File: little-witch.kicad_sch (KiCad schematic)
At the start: 31 parts, among them J1 GCT-USB4105, J3 Conn_ARM_SWD_TagConnect_TC203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, J4 GCT-USB4105, J5 Conn_02x20_Odd_Even, J6 BOOT0_SEL, SW1 SW_Push, U1 CH32V307RCT6, Y1 SIT8008BI-73-33N-25.000000

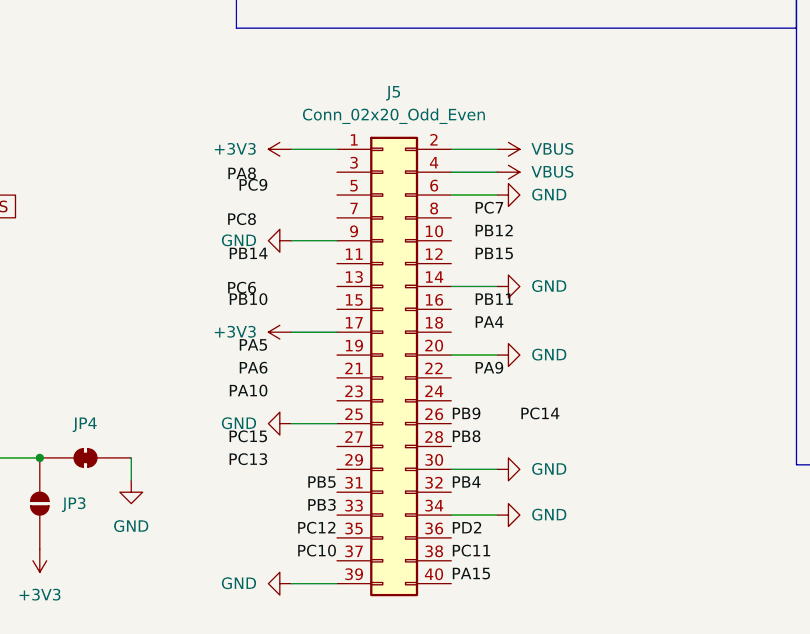
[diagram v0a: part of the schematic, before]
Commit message: More GPIO routing
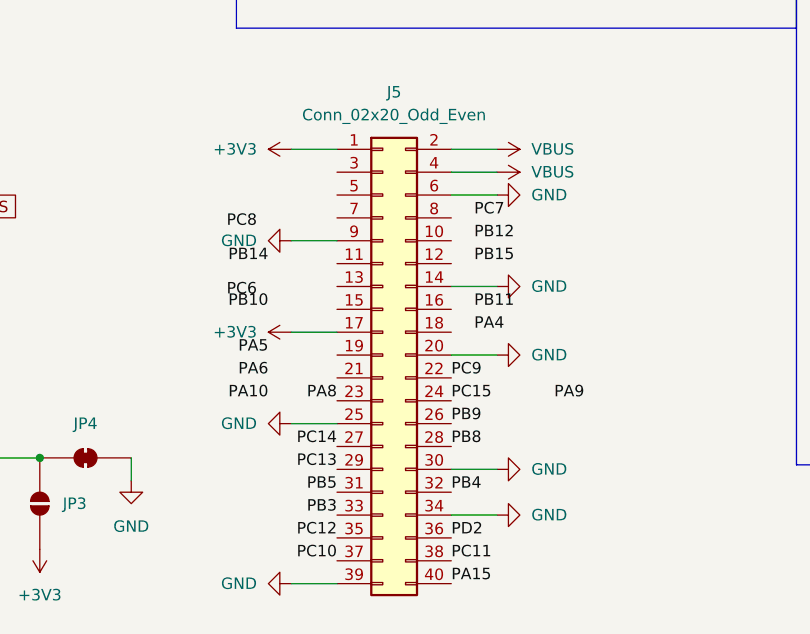
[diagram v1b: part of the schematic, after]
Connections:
- net PA8: now also J5.23 (Pin_23)
- net PC13: now also J5.29 (Pin_29)
- net PC14: now also J5.27 (Pin_27)
- net PC15: now also J5.24 (Pin_24)
- net PC9: now also J5.22 (Pin_22)
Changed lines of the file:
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@@
 	)
 	(label "PC13"
-		(at 162.56 139.7 180)
+		(at 170.18 139.7 180)
 		(effects
 			(font
@@
 	)
 	(label "PC14"
-		(at 190.5 134.62 0)
-		(effects
-			(font
-				(size 1.27 1.27)
-			)
-			(justify left bottom)
+		(at 170.18 137.16 180)
+		(effects
+			(font
+				(size 1.27 1.27)
+			)
+			(justify right bottom)
 		)
 	)
@@
 	)
 	(label "PC15"
-		(at 162.56 137.16 180)
-		(effects
-			(font
-				(size 1.27 1.27)
-			)
-			(justify right bottom)
+		(at 182.88 132.08 0)
+		(effects
+			(font
+				(size 1.27 1.27)
+			)
+			(justify left bottom)
 		)
 	)
@@
 	)
 	(label "PA9"
-		(at 185.42 129.54 0)
+		(at 194.31 132.08 0)
 		(effects
 			(font
@@
 	)
 	(label "PA8"
-		(at 161.29 107.95 180)
+		(at 170.18 132.08 180)
 		(effects
 			(font
@@
 	)
 	(label "PC9"
-		(at 162.56 109.22 180)
-		(effects
-			(font
-				(size 1.27 1.27)
-			)
-			(justify right bottom)
-		)
-	)
+		(at 182.88 129.54 0)
+		(effects
+			(font
+				(size 1.27 1.27)
+			)
+			(justify left bottom)
+		)
+	)

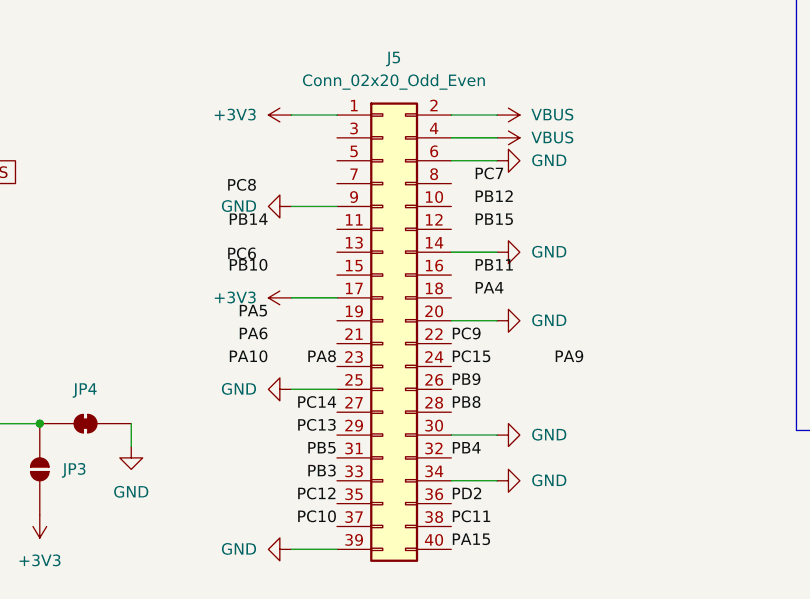
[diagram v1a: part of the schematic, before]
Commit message: Yet more GPIO routing
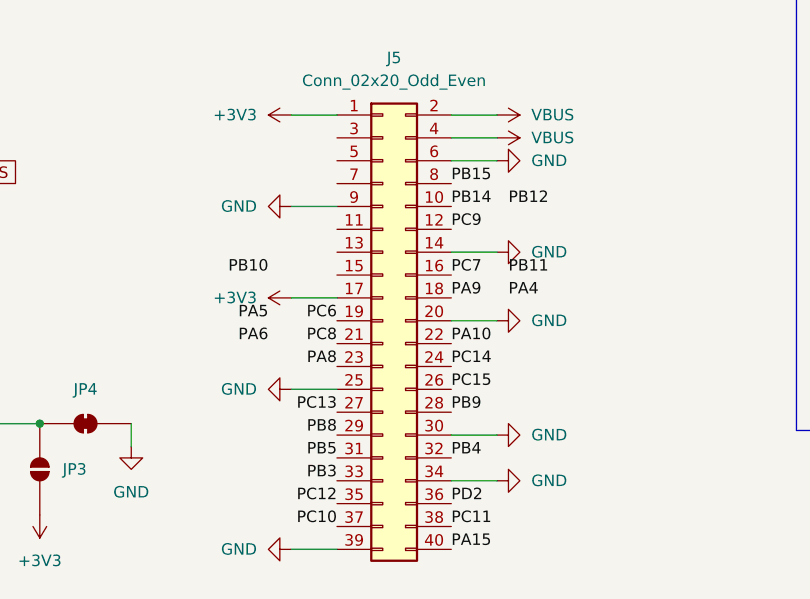
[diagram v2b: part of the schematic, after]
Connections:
- net PA10: now also J5.22 (Pin_22)
- net PA9: now also J5.18 (Pin_18)
- net PB14: now also J5.10 (Pin_10)
- net PB15: now also J5.8 (Pin_8)
- net PB8: now also J5.29 (Pin_29); no longer J5.28 (Pin_28)
- net PB9: now also J5.28 (Pin_28); no longer J5.26 (Pin_26)
- net PC13: now also J5.27 (Pin_27); no longer J5.29 (Pin_29)
- net PC14: now also J5.24 (Pin_24); no longer J5.27 (Pin_27)
- net PC15: now also J5.26 (Pin_26); no longer J5.24 (Pin_24)
- net PC6: now also J5.19 (Pin_19)
- net PC7: now also J5.16 (Pin_16)
- net PC8: now also J5.21 (Pin_21)
- net PC9: now also J5.12 (Pin_12); no longer J5.22 (Pin_22)
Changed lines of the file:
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@@
+		)
+	)
+	(label "PB9"
+		(at 182.88 137.16 0)
+		(effects
+			(font
+				(size 1.27 1.27)
+			)
+			(justify left bottom)
 		)
 	)
@@
 		)
 	)
-	(label "PC13"
-		(at 170.18 139.7 180)
-		(effects
-			(font
-				(size 1.27 1.27)
-			)
-			(justify right bottom)
-		)
-	)
 	(label "PC15"
 		(at 66.04 168.91 180)
@@
 	)
 	(label "PA4"
-		(at 185.42 124.46 0)
+		(at 189.23 124.46 0)
 		(effects
 			(font
@@
 	)
 	(label "PC6"
-		(at 161.29 120.65 180)
+		(at 170.18 127 180)
 		(effects
 			(font
@@
 		)
 	)
-	(label "PC14"
-		(at 170.18 137.16 180)
-		(effects
-			(font
-				(size 1.27 1.27)
-			)
-			(justify right bottom)
-		)
-	)
 	(label "PC8"
 		(at 66.04 151.13 180)
@@
 		)
 	)
+	(label "PB8"
+		(at 170.18 139.7 180)
+		(effects
+			(font
+				(size 1.27 1.27)
+			)
+			(justify right bottom)
+		)
+	)
 	(label "PA6"
 		(at 104.14 102.87 0)
@@
 		)
 	)
-	(label "PC15"
-		(at 182.88 132.08 0)
-		(effects
-			(font
-				(size 1.27 1.27)
-			)
-			(justify left bottom)
-		)
-	)
 	(label "PA10"
 		(at 104.14 113.03 0)
@@
 		)
 	)
-	(label "PB8"
-		(at 182.88 137.16 0)
-		(effects
-			(font
-				(size 1.27 1.27)
-			)
-			(justify left bottom)
-		)
-	)
 	(label "PA10"
-		(at 162.56 132.08 180)
-		(effects
-			(font
-				(size 1.27 1.27)
-			)
-			(justify right bottom)
+		(at 182.88 129.54 0)
+		(effects
+			(font
+				(size 1.27 1.27)
+			)
+			(justify left bottom)
 		)
 	)
 	(label "PA9"
-		(at 194.31 132.08 0)
+		(at 182.88 124.46 0)
 		(effects
 			(font
@@
 	)
 	(label "PC7"
-		(at 185.42 111.76 0)
+		(at 182.88 121.92 0)
 		(effects
 			(font
@@
 	)
 	(label "PB15"
-		(at 185.42 116.84 0)
+		(at 182.88 111.76 0)
 		(effects
 			(font
@@
 	)
 	(label "PB12"
-		(at 185.42 114.3 0)
+		(at 189.23 114.3 0)
 		(effects
 			(font
@@
 		)
 	)
-	(label "PB9"
-		(at 182.88 134.62 0)
-		(effects
-			(font
-				(size 1.27 1.27)
-			)
-			(justify left bottom)
-		)
-	)
 	(label "PB11"
-		(at 185.42 121.92 0)
+		(at 189.23 121.92 0)
 		(effects
 			(font
@@
 		)
 	)
+	(label "PC13"
+		(at 170.18 137.16 180)
+		(effects
+			(font
+				(size 1.27 1.27)
+			)
+			(justify right bottom)
+		)
+	)
 	(label "PB2"
 		(at 104.14 135.89 0)
@@
 	)
 	(label "PC8"
-		(at 161.29 113.03 180)
+		(at 170.18 129.54 180)
 		(effects
 			(font
@@
 	)
 	(label "PB14"
-		(at 162.56 116.84 180)
-		(effects
-			(font
-				(size 1.27 1.27)
-			)
-			(justify right bottom)
+		(at 182.88 114.3 0)
+		(effects
+			(font
+				(size 1.27 1.27)
+			)
+			(justify left bottom)
+		)
+	)
+	(label "PC15"
+		(at 182.88 134.62 0)
+		(effects
+			(font
+				(size 1.27 1.27)
+			)
+			(justify left bottom)
+		)
+	)
+	(label "PC9"
+		(at 182.88 116.84 0)
+		(effects
+			(font
+				(size 1.27 1.27)
+			)
+			(justify left bottom)
 		)
 	)
@@
 		)
 	)
-	(label "PC9"
-		(at 182.88 129.54 0)
-		(effects
-			(font
+	(label "PC14"
+		(at 182.88 132.08 0)
+		(effects
+			(font

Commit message: GPIO fully routed
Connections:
- net PA4: now also J5.7 (Pin_7)
- net PA5: now also J5.5 (Pin_5)
- net PA6: now also J5.3 (Pin_3)
- net PB1: now also J5.11 (Pin_11)
- net PB10: now also J5.13 (Pin_13)
- net PB11: now also J5.15 (Pin_15)
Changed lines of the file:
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@@
 	)
 	(label "PB10"
-		(at 162.56 121.92 180)
+		(at 170.18 119.38 180)
 		(effects
 			(font
@@
 	)
 	(label "PA5"
-		(at 162.56 127 180)
+		(at 170.18 109.22 180)
 		(effects
 			(font
@@
 		)
 	)
+	(label "PB1"
+		(at 170.18 116.84 180)
+		(effects
+			(font
+				(size 1.27 1.27)
+			)
+			(justify right bottom)
+		)
+	)
 	(label "PA3"
 		(at 104.14 95.25 0)
@@
 	)
 	(label "PA6"
-		(at 162.56 129.54 180)
+		(at 170.18 106.68 180)
 		(effects
 			(font
@@
 	)
 	(label "PA4"
-		(at 189.23 124.46 0)
-		(effects
-			(font
-				(size 1.27 1.27)
-			)
-			(justify left bottom)
+		(at 170.18 111.76 180)
+		(effects
+			(font
+				(size 1.27 1.27)
+			)
+			(justify right bottom)
 		)
 	)
@@
 		)
 	)
-	(label "PB12"
-		(at 189.23 114.3 0)
-		(effects
-			(font
-				(size 1.27 1.27)
-			)
-			(justify left bottom)
-		)
-	)
 	(label "PB4"
 		(at 182.88 142.24 0)
@@
 	)
 	(label "PB11"
-		(at 189.23 121.92 0)
-		(effects
-			(font
-				(size 1.27 1.27)
-			)
-			(justify left bottom)
-		)
-	)
+		(at 170.18 121.92 180)
+		(effects
+			(font
+				(size 1.27 1.27)
+			)
+			(justify right bottom)
+		)
+	)

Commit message: Better GPIO routing
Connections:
- net PA10: now also J5.18 (Pin_18); no longer J5.22 (Pin_22)
- net PA8: now also J5.12 (Pin_12); no longer J5.23 (Pin_23)
- net PA9: now also J5.22 (Pin_22); no longer J5.18 (Pin_18)
- net PC7: now also J5.21 (Pin_21); no longer J5.16 (Pin_16)
- net PC8: now also J5.23 (Pin_23); no longer J5.21 (Pin_21)
- net PC9: now also J5.16 (Pin_16); no longer J5.12 (Pin_12)

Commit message: Power regulation
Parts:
- removed R1: 10k, Resistor_SMD:R_0402_1005Metric, symbol Device:R_Small_US
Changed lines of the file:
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@@
 	)
 	(junction
-		(at 57.15 87.63)
-		(diameter 0)
-		(color 0 0 0 0)
-	)
-	(junction
 		(at 82.55 76.2)
 		(diameter 0)
@@
 	(wire
 		(pts
-			(xy 57.15 87.63) (xy 67.31 87.63)
+			(xy 49.53 87.63) (xy 67.31 87.63)
 		)
 		(stroke
@@
 	(wire
 		(pts
-			(xy 57.15 85.09) (xy 57.15 87.63)
-		)
-		(stroke
-			(width 0)
-			(type default)
-		)
-	)
-	(wire
-		(pts
 			(xy 185.42 30.48) (xy 194.31 30.48)
 		)
@@
 	(wire
 		(pts
-			(xy 49.53 87.63) (xy 57.15 87.63)
-		)
-		(stroke
-			(width 0)
-			(type default)
-		)
-	)
-	(wire
-		(pts
 			(xy 102.87 135.89) (xy 115.57 135.89)
 		)
@@
 	(wire
 		(pts
-			(xy 57.15 77.47) (xy 57.15 80.01)
-		)
-		(stroke
-			(width 0)
-			(type default)
-		)
-	)
-	(wire
-		(pts
 			(xy 90.17 76.2) (xy 92.71 76.2)
 		)
@@
 	)
 	(symbol
-		(lib_id "power:+3V3")
-		(at 57.15 77.47 0)
-		(unit 1)
-		(body_style 1)
-		(exclude_from_sim no)
-		(in_bom yes)
-		(on_board yes)
-		(in_pos_files yes)
-		(dnp no)
-		(fields_autoplaced yes)
-		(property "Reference" "#PWR08"
-			(at 57.15 81.28 0)
-			(hide yes)
-			(show_name no)
-			(do_not_autoplace no)
-			(effects
-				(font
-					(size 1.27 1.27)
-				)
-			)
-		)
-		(property "Value" "+3V3"
-			(at 57.15 72.39 0)
-			(show_name no)
-			(do_not_autoplace no)
-			(effects
-				(font
-					(size 1.27 1.27)
-				)
-			)
-		)
-		(property "Footprint" ""
-			(at 57.15 77.47 0)
-			(hide yes)
-			(show_name no)
-			(do_not_autoplace no)
-			(effects
-				(font
-					(size 1.27 1.27)
-				)
-			)
-		)
-		(property "Datasheet" ""
-			(at 57.15 77.47 0)
-			(hide yes)
-			(show_name no)
-			(do_not_autoplace no)
-			(effects
-				(font
-					(size 1.27 1.27)
-				)
-			)
-		)
-		(property "Description" "Power symbol creates a global label with name \"+3V3\""
-			(at 57.15 77.47 0)
-			(hide yes)
-			(show_name no)
-			(do_not_autoplace no)
-			(effects
-				(font
-					(size 1.27 1.27)
-				)
-			)
-		)
-		(pin "1"
-		)
-		(instances
-			(project "little-witch"
-				(path "/eaea4e42-a070-4be5-b9dd-9215ef3d72c7"
-					(reference "#PWR08")
-					(unit 1)
-				)
-			)
-		)
-	)
-	(symbol
 		(lib_id "Mechanical:MountingHole_Pad")
 		(at 194.31 27.94 0)
@@
 					(unit 1)
 				)
-			)
-		)
-	)
-	(symbol
-		(lib_id "Device:R_Small_US")
-		(at 57.15 82.55 0)
-		(unit 1)
-		(body_style 1)
-		(exclude_from_sim no)
-		(in_bom yes)
-		(on_board yes)
-		(in_pos_files yes)
-		(dnp no)
-		(fields_autoplaced yes)
-		(property "Reference" "R1"
-			(at 59.69 81.2799 0)
-			(show_name no)
-			(do_not_autoplace no)
-			(effects
-				(font
-					(size 1.27 1.27)
-				)
-				(justify left)
-			)
-		)
-		(property "Value" "10k"
-			(at 59.69 83.8199 0)
-			(show_name no)
-			(do_not_autoplace no)
-			(effects
-				(font
-					(size 1.27 1.27)
-				)
-				(justify left)
-			)
-		)
-		(property "Footprint" "Resistor_SMD:R_0402_1005Metric"
-			(at 57.15 82.55 0)
-			(hide yes)
-			(show_name no)
-			(do_not_autoplace no)
-			(effects
-				(font
-					(size 1.27 1.27)
-				)
-			)
-		)
-		(property "Datasheet" ""
-			(at 57.15 82.55 0)
-			(hide yes)
-			(show_name no)
-			(do_not_autoplace no)
-			(effects
-				(font
-					(size 1.27 1.27)
-				)
-			)
-		)
-		(property "Description" "Resistor, small US symbol"
-			(at 57.15 82.55 0)
-			(hide yes)
-			(show_name no)
-			(do_not_autoplace no)
-			(effects
-				(font
-					(size 1.27 1.27)
-				)
-			)
-		)
-		(pin "2"
-		)
-		(pin "1"
-		)
-		(instances
-			(project "little-witch"
-				(path "/eaea4e42-a070-4be5-b9dd-9215ef3d72c7"
-					(reference "R1")
-					(unit 1)
-				)

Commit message: Debug routing
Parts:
- removed J6: BOOT0_SEL, Connector_PinHeader_2.54mm:PinHeader_1x03_P2.54mm_Vertical, symbol Connector_Generic:Conn_01x03
- added C14: 100n, Capacitor_SMD:C_0402_1005Metric, symbol Device:C_Small_US
- added SW2: BOOT0, Button_Switch_SMD:SW_Push_1P1T_NO_CK_KMR2, symbol Switch:SW_Push
- SW1: value SW_Push -> RESET
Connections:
- net +3V3: now also C14.1, SW2.1
- net GND: now also R10.1
- net at R10.2, U1.60 (BOOT0): now also C14.2, SW2.2
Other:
- moved on the sheet: R10

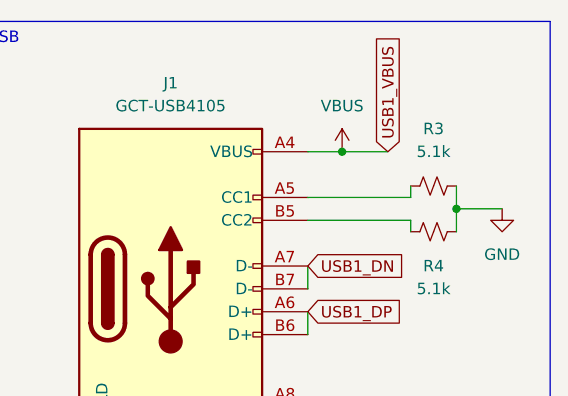
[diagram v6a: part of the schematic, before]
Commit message: USB VBUS diode
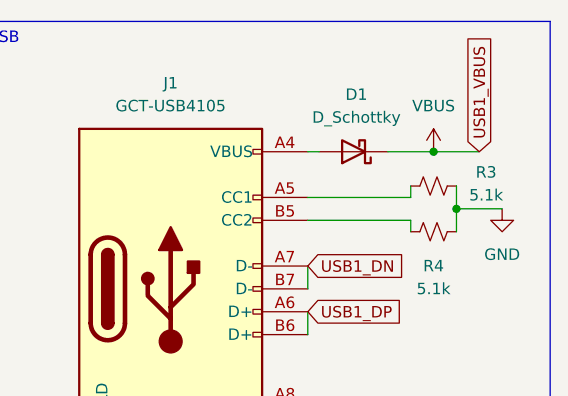
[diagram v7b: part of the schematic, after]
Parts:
- added D1: D_Schottky, symbol Device:D_Schottky
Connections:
- net VBUS: now also D1.1 (K); no longer J1.A4 (VBUS), J1.A9 (VBUS), J1.B4 (VBUS), J1.B9 (VBUS)
- new net: D1.2 (A), J1.A4 (VBUS), J1.A9 (VBUS), J1.B4 (VBUS), J1.B9 (VBUS)
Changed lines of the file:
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@@
 	)
 	(junction
-		(at 261.62 26.67)
-		(diameter 0)
-		(color 0 0 0 0)
-	)
-	(junction
 		(at 73.66 22.86)
 		(diameter 0)
@@
 	)
 	(junction
+		(at 271.78 26.67)
+		(diameter 0)
+		(color 0 0 0 0)
+	)
+	(junction
 		(at 90.17 76.2)
 		(diameter 0)
@@
 	(wire
 		(pts
-			(xy 257.81 26.67) (xy 261.62 26.67)
+			(xy 257.81 26.67) (xy 259.08 26.67)
 		)
 		(stroke
@@
 	(wire
 		(pts
+			(xy 266.7 26.67) (xy 271.78 26.67)
+		)
+		(stroke
+			(width 0)
+			(type default)
+		)
+	)
+	(wire
+		(pts
 			(xy 16.51 22.86) (xy 16.51 25.4)
 		)
@@
 	(wire
 		(pts
-			(xy 261.62 26.67) (xy 266.7 26.67)
+			(xy 271.78 26.67) (xy 276.86 26.67)
 		)
 		(stroke
@@
 	(global_label "USB1_VBUS"
 		(shape input)
-		(at 266.7 26.67 90)
+		(at 276.86 26.67 90)
 		(fields_autoplaced yes)
 		(effects
@@
 		)
 		(property "Intersheetrefs" "${INTERSHEET_REFS}"
-			(at 266.7 12.7991 90)
+			(at 276.86 12.7991 90)
 			(hide yes)
 			(show_name no)
@@
 	(symbol
 		(lib_id "power:VBUS")
-		(at 261.62 26.67 0)
+		(at 271.78 26.67 0)
 		(unit 1)
 		(body_style 1)
@@
 		(fields_autoplaced yes)
 		(property "Reference" "#PWR021"
-			(at 261.62 30.48 0)
+			(at 271.78 30.48 0)
 			(hide yes)
 			(show_name no)
@@
 		)
 		(property "Value" "VBUS"
-			(at 261.62 21.59 0)
+			(at 271.78 21.59 0)
 			(show_name no)
 			(do_not_autoplace no)
@@
 		)
 		(property "Footprint" ""
-			(at 261.62 26.67 0)
+			(at 271.78 26.67 0)
 			(hide yes)
 			(show_name no)
@@
 		)
 		(property "Datasheet" ""
-			(at 261.62 26.67 0)
+			(at 271.78 26.67 0)
 			(hide yes)
 			(show_name no)
@@
 		)
 		(property "Description" "Power symbol creates a global label with name \"VBUS\""
-			(at 261.62 26.67 0)
+			(at 271.78 26.67 0)
 			(hide yes)
 			(show_name no)
@@
 	)
 	(symbol
+		(lib_id "Device:D_Schottky")
+		(at 262.89 26.67 180)
+		(unit 1)
+		(body_style 1)
+		(exclude_from_sim no)
+		(in_bom yes)
+		(on_board yes)
+		(in_pos_files yes)
+		(dnp no)
+		(fields_autoplaced yes)
+		(property "Reference" "D1"
+			(at 263.2075 20.32 0)
+			(show_name no)
+			(do_not_autoplace no)
+			(effects
+				(font
+					(size 1.27 1.27)
+				)
+			)
+		)
+		(property "Value" "D_Schottky"
+			(at 263.2075 22.86 0)
+			(show_name no)
+			(do_not_autoplace no)
+			(effects
+				(font
+					(size 1.27 1.27)
+				)
+			)
+		)
+		(property "Footprint" ""
+			(at 262.89 26.67 0)
+			(hide yes)
+			(show_name no)
+			(do_not_autoplace no)
+			(effects
+				(font
+					(size 1.27 1.27)
+				)
+			)
+		)
+		(property "Datasheet" ""
+			(at 262.89 26.67 0)
+			(hide yes)
+			(show_name no)
+			(do_not_autoplace no)
+			(effects
+				(font
+					(size 1.27 1.27)
+				)
+			)
+		)
+		(property "Description" "Schottky diode"
+			(at 262.89 26.67 0)
+			(hide yes)
+			(show_name no)
+			(do_not_autoplace no)
+			(effects
+				(font
+					(size 1.27 1.27)
+				)
+			)
+		)
+		(pin "2"
+		)
+		(pin "1"
+		)
+		(instances
+			(project "little-witch"
+				(path "/eaea4e42-a070-4be5-b9dd-9215ef3d72c7"
+					(reference "D1")
+					(unit 1)
+				)
+			)
+		)
+	)
+	(symbol
 		(lib_id "Switch:SW_Push")
 		(at 43.18 101.6 0)
@@
 		(in_pos_files yes)
 		(dnp no)
-		(fields_autoplaced yes)
 		(property "Reference" "R3"
-			(at 271.78 24.13 90)
+			(at 277.622 28.956 90)
 			(show_name no)
 			(do_not_autoplace no)
@@
 		)
 		(property "Value" "5.1k"
-			(at 271.78 26.67 90)
+			(at 277.622 31.496 90)
 			(show_name no)
 			(do_not_autoplace no)
